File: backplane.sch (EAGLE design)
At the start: 45 parts, among them J1 L717HDE15PD4CH4R, J10 5013310807, J11 5013310807, J12 5013310807, J13 5013310807, J14 5013311007, J15 5013311007, J16 5013311007, J17 5013311007, J18 5013311007, J19 5013311007, J2 1054301102, J20 5013311007, J21 5013311007, J22 5013311007, J23 5013311007, J24 SEAM-40-03.0-S-06-2-A-K-TR, J25 5055670271, J3 5011902017, J4 5013310807, J5 5013310807, J6 5013310807, J7 5013310807, J8 5013310807, J9 5013310807, U1 AM26LV32EIPWR, U10 AM26LV32EIPWR, U2 AM26LV32EIPWR, U3 AM26LV32EIPWR, U4 AM26LV32EIPWR, U5 AM26LV32EIPWR, U6 AM26LV32EIPWR, U7 AM26LV32EIPWR, U8 AM26LV32EIPWR, U9 AM26LV32EIPWR

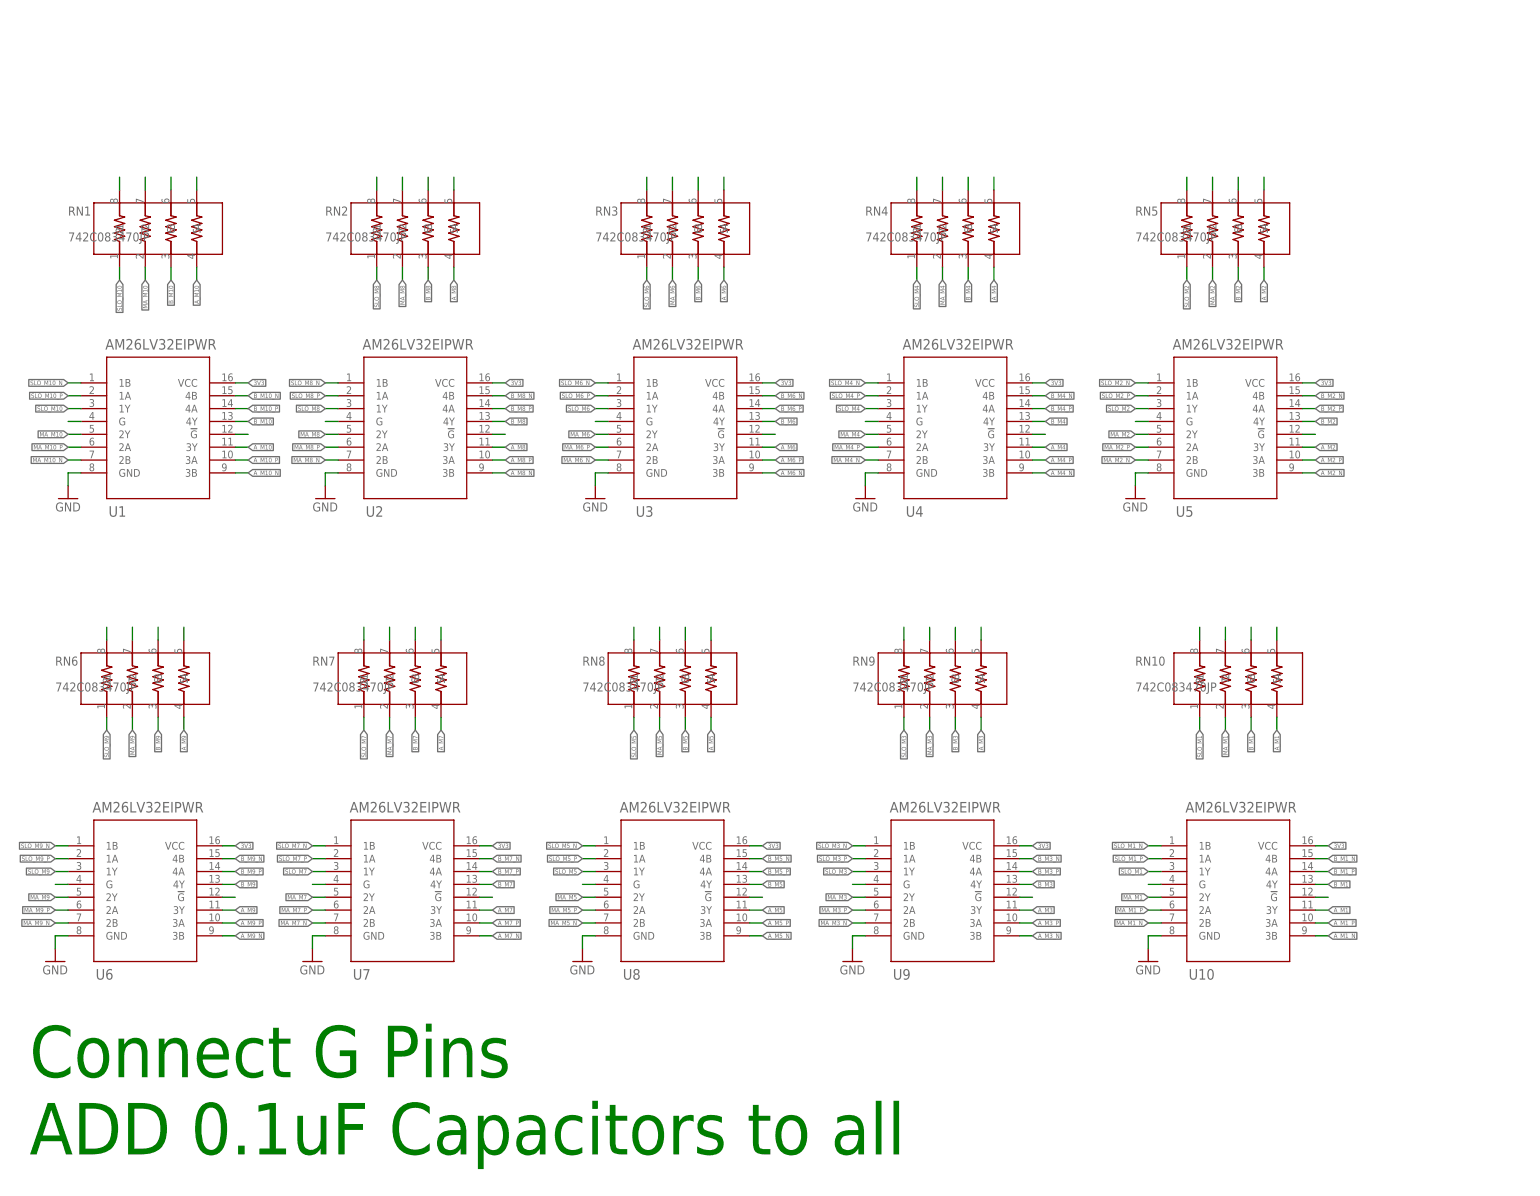
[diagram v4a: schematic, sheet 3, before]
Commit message: Routed power to AMC/encoder connectors and drivers
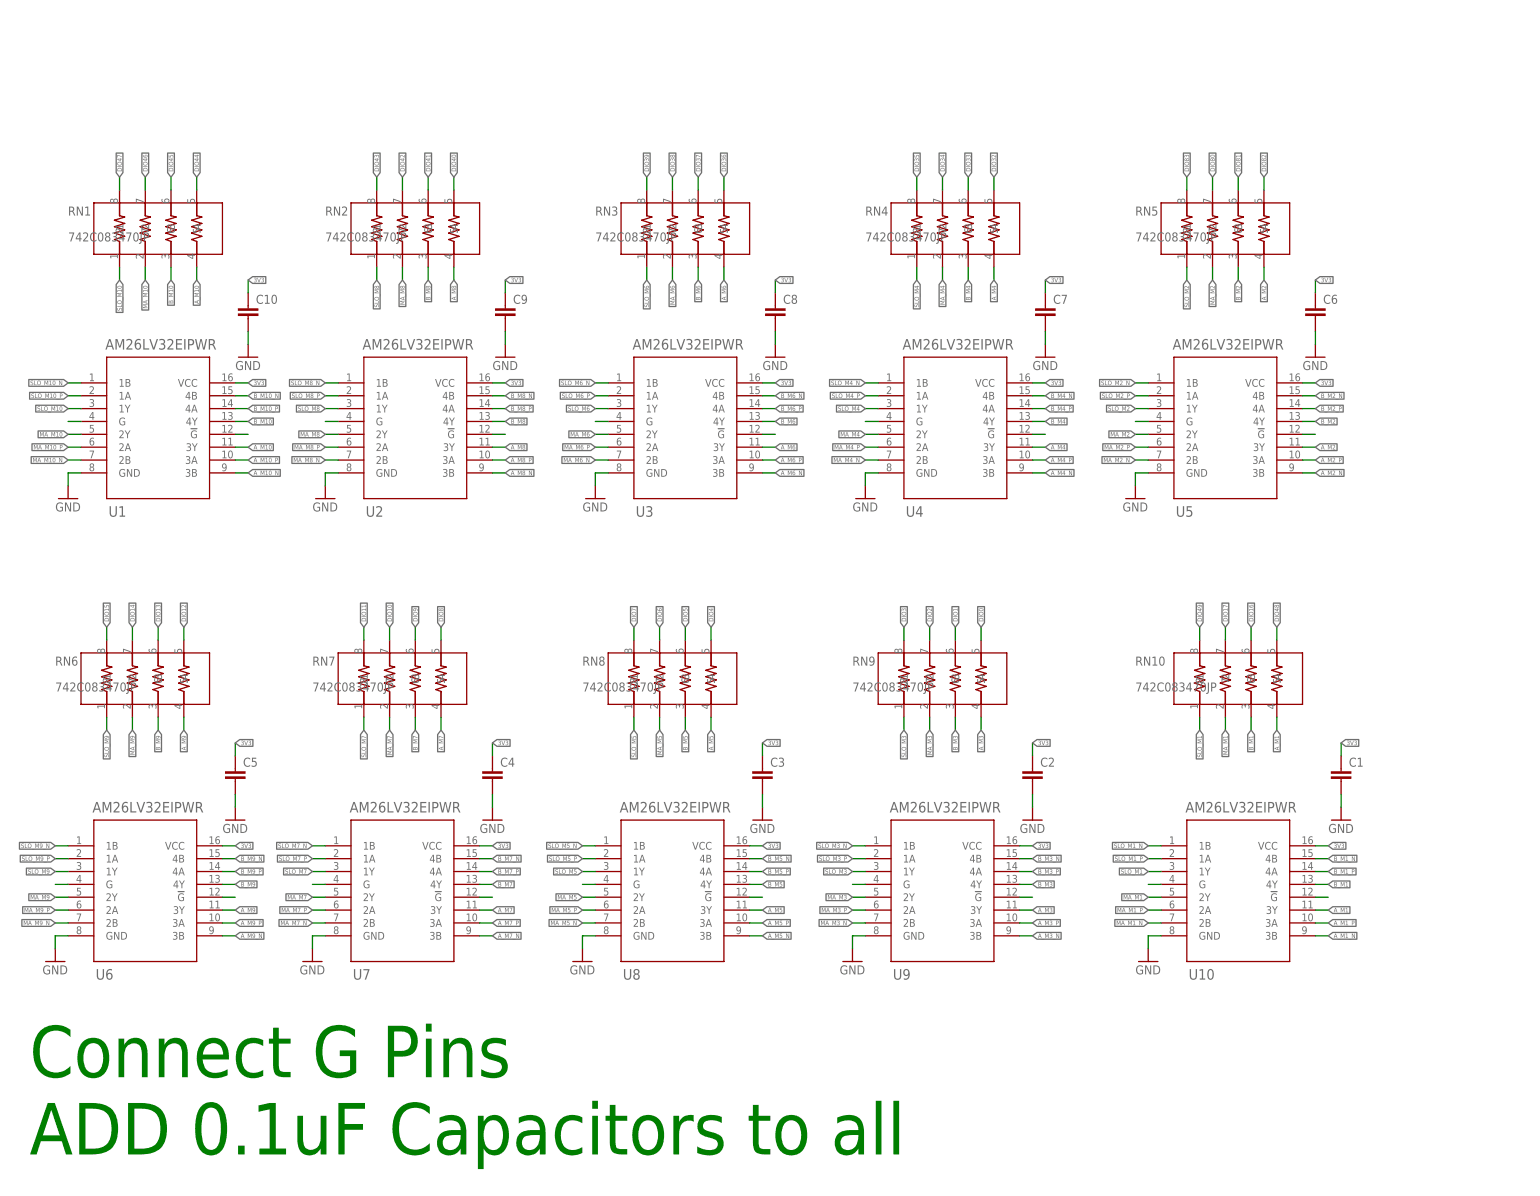
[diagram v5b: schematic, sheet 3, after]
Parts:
- added C1, C10, C2, C3, C4, C5, C6, C7, C8, C9: (no value), rcl:C-EUC0603
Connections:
- removed net N$1: RN9.5
- removed net N$10: RN10.7
- removed net N$11: RN10.8
- removed net N$12: RN8.7
- removed net N$14: RN8.8
- removed net N$15: RN7.5
- removed net N$16: RN7.6
- removed net N$17: RN7.7
- removed net N$18: RN7.8
- removed net N$19: RN6.5
- removed net N$2: RN9.6
- removed net N$20: RN6.6
- removed net N$21: RN6.7
- removed net N$22: RN6.8
- removed net N$24: RN5.5
- removed net N$25: RN5.6
- removed net N$26: RN5.7
- removed net N$27: RN5.8
- removed net N$28: RN4.5
- removed net N$29: RN4.6
- removed net N$3: RN9.7
- removed net N$31: RN4.7
- removed net N$32: RN4.8
- removed net N$33: RN3.5
- removed net N$34: RN3.6
- removed net N$35: RN3.7
- removed net N$36: RN3.8
- removed net N$38: RN2.5
- removed net N$39: RN2.6
- removed net N$40: RN2.7
- removed net N$41: RN2.8
- removed net N$42: RN1.5
- removed net N$43: RN1.6
- removed net N$45: RN1.7
- removed net N$46: RN1.8
- removed net N$5: RN9.8
- removed net N$6: RN8.5
- removed net N$7: RN8.6
- removed net N$8: RN10.5
- removed net N$9: RN10.6
- net 3V3: now also C1.1, C10.1, C2.1, C3.1, C4.1, C5.1, C6.1, C7.1, C8.1, C9.1
- net DIO0: now also RN9.5
- net DIO1: now also RN9.6
- net DIO10: now also RN7.7
- net DIO11: now also RN7.8
- net DIO12: now also RN6.5
- net DIO13: now also RN6.6
- net DIO14: now also RN6.7
- net DIO15: now also RN6.8
- net DIO16: now also RN10.6
- net DIO17: now also RN10.7
- net DIO2: now also RN9.7
- net DIO3: now also RN9.8
- net DIO32: now also RN4.5
- net DIO33: now also RN4.6
- net DIO34: now also RN4.7
- net DIO35: now also RN4.8
- net DIO36: now also RN3.5
- net DIO37: now also RN3.6
- net DIO38: now also RN3.7
- net DIO39: now also RN3.8
- net DIO4: now also RN8.5
- net DIO40: now also RN2.5
- net DIO41: now also RN2.6
- net DIO42: now also RN2.7
- net DIO43: now also RN2.8
- net DIO44: now also RN1.5
- net DIO45: now also RN1.6
- net DIO46: now also RN1.7
- net DIO47: now also RN1.8
- net DIO48: now also RN10.5
- net DIO49: now also RN10.8
- net DIO5: now also RN8.6
- net DIO6: now also RN8.7
- net DIO7: now also RN8.8
- net DIO8: now also RN7.5
- net DIO80: now also RN5.7
- net DIO81: now also RN5.6
- net DIO82: now also RN5.5
- net DIO83: now also RN5.8
- net DIO9: now also RN7.6
- net ESTP+: now also J25.2
- net ESTP-: now also J25.1
- net GND: now also C1.2, C10.2, C2.2, C3.2, C4.2, C5.2, C6.2, C7.2, C8.2, C9.2, J25.3, J25.4

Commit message: added bypass caps and routed G pins on drivers
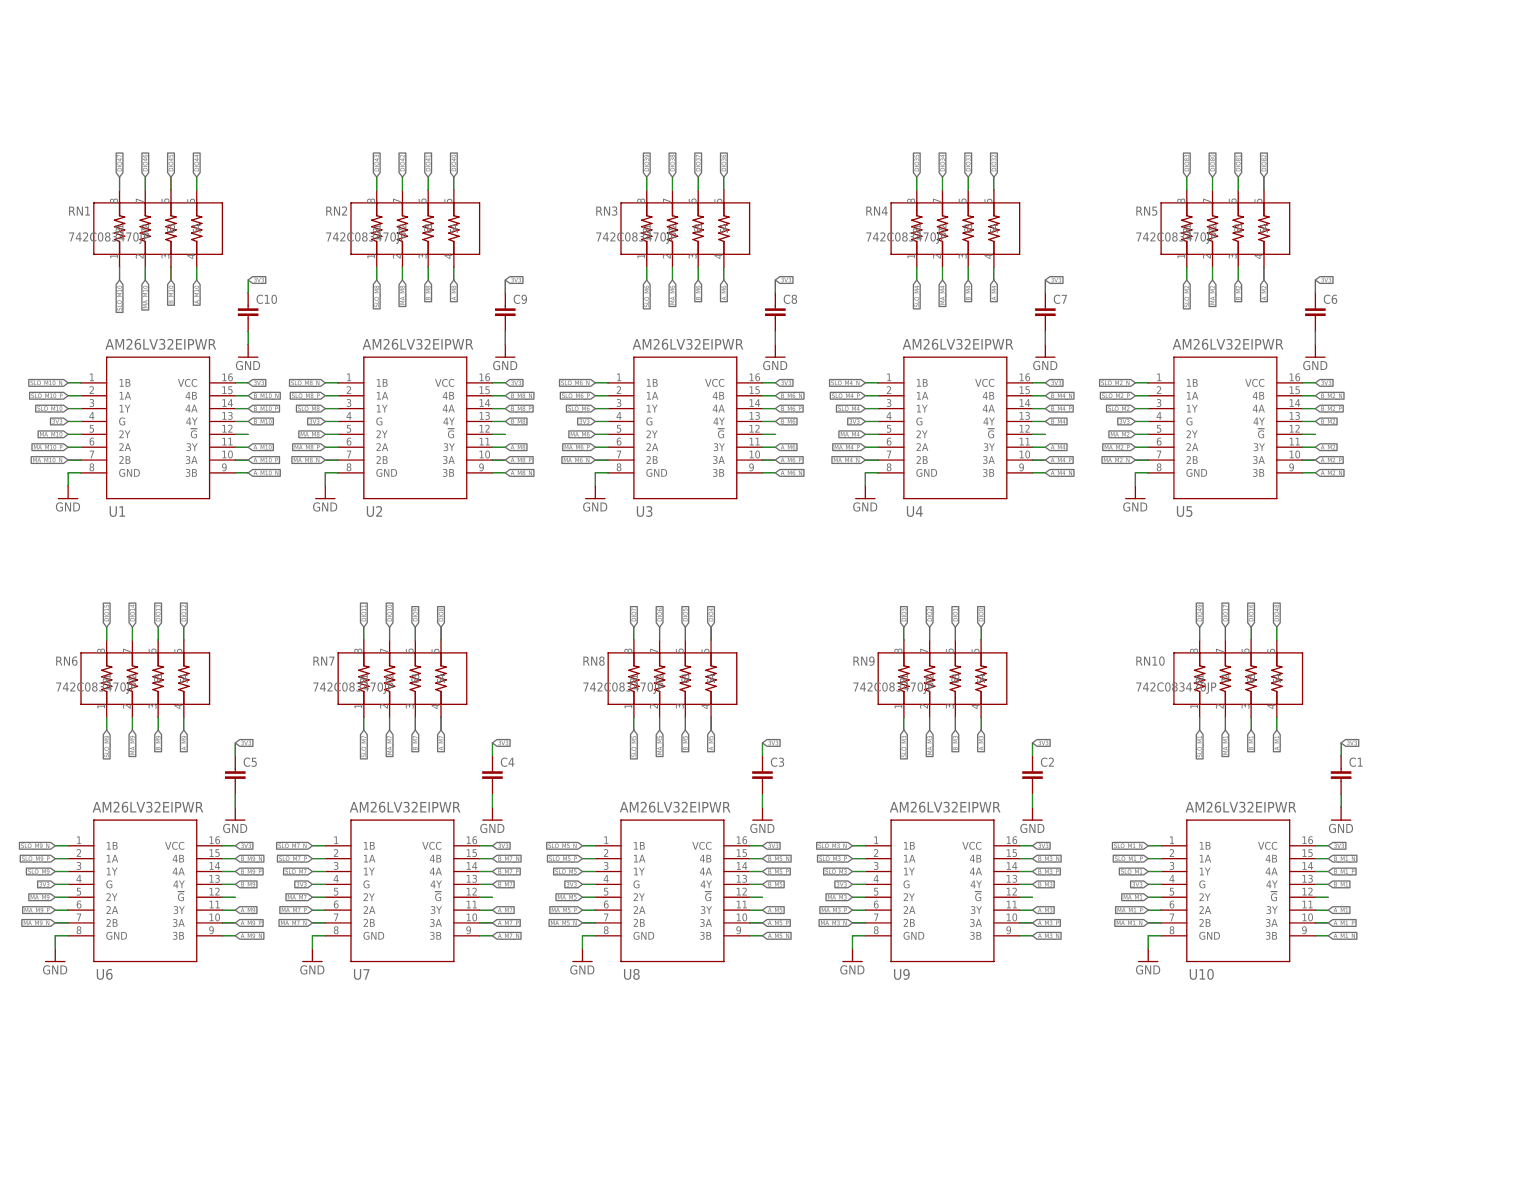
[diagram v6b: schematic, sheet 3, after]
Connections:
- removed net N$108: U4.G
- removed net N$124: U3.G
- removed net N$13: U10.G
- removed net N$140: U2.G
- removed net N$156: U1.G
- removed net N$30: U9.G
- removed net N$44: U8.G
- removed net N$60: U7.G
- removed net N$76: U6.G
- removed net N$92: U5.G
- net 3V3: now also U1.G, U10.G, U2.G, U3.G, U4.G, U5.G, U6.G, U7.G, U8.G, U9.G
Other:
- note removed: "ADD 0.1uF Capacitors to all"
- note removed: "Connect G Pins"
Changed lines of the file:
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@@
 <sheet>
 <plain>
-<text x="10.16" y="20.32" size="10.16" layer="91">Connect G Pins</text>
-<text x="10.16" y="5.08" size="10.16" layer="91">ADD 0.1uF Capacitors to all</text>
 </plain>
 <instances>
@@
 <label x="53.34" y="177.8" size="0.889" layer="95" xref="yes"/>
 </segment>
+<segment>
+<pinref part="U4" gate="A" pin="G"/>
+<wire x1="177.8" y1="149.86" x2="175.26" y2="149.86" width="0.1524" layer="91"/>
+<label x="175.26" y="149.86" size="0.889" layer="95" rot="R180" xref="yes"/>
+</segment>
+<segment>
+<pinref part="U5" gate="A" pin="G"/>
+<wire x1="231.14" y1="149.86" x2="228.6" y2="149.86" width="0.1524" layer="91"/>
+<label x="228.6" y="149.86" size="0.889" layer="95" rot="R180" xref="yes"/>
+</segment>
+<segment>
+<pinref part="U3" gate="A" pin="G"/>
+<wire x1="124.46" y1="149.86" x2="121.92" y2="149.86" width="0.1524" layer="91"/>
+<label x="121.92" y="149.86" size="0.889" layer="95" rot="R180" xref="yes"/>
+</segment>
+<segment>
+<pinref part="U2" gate="A" pin="G"/>
+<wire x1="71.12" y1="149.86" x2="68.58" y2="149.86" width="0.1524" layer="91"/>
+<label x="68.58" y="149.86" size="0.889" layer="95" rot="R180" xref="yes"/>
+</segment>
+<segment>
+<pinref part="U1" gate="A" pin="G"/>
+<wire x1="20.32" y1="149.86" x2="17.78" y2="149.86" width="0.1524" layer="91"/>
+<label x="17.78" y="149.86" size="0.889" layer="95" rot="R180" xref="yes"/>
+</segment>
+<segment>
+<pinref part="U6" gate="A" pin="G"/>
+<wire x1="17.78" y1="58.42" x2="15.24" y2="58.42" width="0.1524" layer="91"/>
+<label x="15.24" y="58.42" size="0.889" layer="95" rot="R180" xref="yes"/>
+</segment>
+<segment>
+<pinref part="U7" gate="A" pin="G"/>
+<wire x1="68.58" y1="58.42" x2="66.04" y2="58.42" width="0.1524" layer="91"/>
+<label x="66.04" y="58.42" size="0.889" layer="95" rot="R180" xref="yes"/>
+</segment>
+<segment>
+<pinref part="U8" gate="A" pin="G"/>
+<wire x1="121.92" y1="58.42" x2="119.38" y2="58.42" width="0.1524" layer="91"/>
+<label x="119.38" y="58.42" size="0.889" layer="95" rot="R180" xref="yes"/>
+</segment>
+<segment>
+<pinref part="U9" gate="A" pin="G"/>
+<wire x1="175.26" y1="58.42" x2="172.72" y2="58.42" width="0.1524" layer="91"/>
+<label x="172.72" y="58.42" size="0.889" layer="95" rot="R180" xref="yes"/>
+</segment>
+<segment>
+<pinref part="U10" gate="A" pin="G"/>
+<wire x1="233.68" y1="58.42" x2="231.14" y2="58.42" width="0.1524" layer="91"/>
+<label x="231.14" y="58.42" size="0.889" layer="95" rot="R180" xref="yes"/>
+</segment>
 </net>
 <net name="MA_M1_N" class="1">
@@
 </segment>
 </net>
-<net name="N$13" class="0">
-<segment>
-<pinref part="U10" gate="A" pin="G"/>
-<wire x1="233.68" y1="58.42" x2="231.14" y2="58.42" width="0.1524" layer="91"/>
-</segment>
-</net>
 <net name="SLO_M1" class="0">
 <segment>
@@
 </segment>
 </net>
-<net name="N$30" class="0">
-<segment>
-<pinref part="U9" gate="A" pin="G"/>
-<wire x1="175.26" y1="58.42" x2="172.72" y2="58.42" width="0.1524" layer="91"/>
-</segment>
-</net>
 <net name="SLO_M3_P" class="1">
 <segment>
@@
 </segment>
 </net>
-<net name="N$44" class="0">
-<segment>
-<pinref part="U8" gate="A" pin="G"/>
-<wire x1="121.92" y1="58.42" x2="119.38" y2="58.42" width="0.1524" layer="91"/>
-</segment>
-</net>
 <net name="SLO_M5" class="0">
 <segment>
@@
 </segment>
 </net>
-<net name="N$60" class="0">
-<segment>
-<pinref part="U7" gate="A" pin="G"/>
-<wire x1="68.58" y1="58.42" x2="66.04" y2="58.42" width="0.1524" layer="91"/>
-</segment>
-</net>
 <net name="SLO_M7" class="0">
 <segment>
@@
 </segment>
 </net>
-<net name="N$76" class="0">
-<segment>
-<pinref part="U6" gate="A" pin="G"/>
-<wire x1="17.78" y1="58.42" x2="15.24" y2="58.42" width="0.1524" layer="91"/>
-</segment>
-</net>
 <net name="SLO_M9" class="0">
 <segment>
@@
 </segment>
 </net>
-<net name="N$92" class="0">
-<segment>
-<pinref part="U5" gate="A" pin="G"/>
-<wire x1="231.14" y1="149.86" x2="228.6" y2="149.86" width="0.1524" layer="91"/>
-</segment>
-</net>
 <net name="SLO_M2" class="0">
 <segment>
@@
 </segment>
 </net>
-<net name="N$108" class="0">
-<segment>
-<pinref part="U4" gate="A" pin="G"/>
-<wire x1="177.8" y1="149.86" x2="175.26" y2="149.86" width="0.1524" layer="91"/>
-</segment>
-</net>
 <net name="SLO_M4" class="0">
 <segment>
@@
 </segment>
 </net>
-<net name="N$124" class="0">
-<segment>
-<pinref part="U3" gate="A" pin="G"/>
-<wire x1="124.46" y1="149.86" x2="121.92" y2="149.86" width="0.1524" layer="91"/>
-</segment>
-</net>
 <net name="SLO_M6" class="0">
 <segment>
@@
 <wire x1="83.82" y1="180.34" x2="83.82" y2="177.8" width="0.1524" layer="91"/>
 <label x="83.82" y="177.8" size="0.889" layer="95" rot="R270" xref="yes"/>
-</segment>
-</net>
-<net name="N$140" class="0">
-<segment>
-<pinref part="U2" gate="A" pin="G"/>
-<wire x1="71.12" y1="149.86" x2="68.58" y2="149.86" width="0.1524" layer="91"/>
 </segment>
 </net>
@@
 </segment>
 </net>
-<net name="N$156" class="0">
-<segment>
-<pinref part="U1" gate="A" pin="G"/>
-<wire x1="20.32" y1="149.86" x2="17.78" y2="149.86" width="0.1524" layer="91"/>
-</segment>
-</net>
